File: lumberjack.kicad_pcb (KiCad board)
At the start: 2 copper layers, 284.7 x 94.2 mm, 164 parts, among them J1 USB, J2 AVR_ISP_6, J3 JST, J4 JST, SW1 RESET, SW2 BOOT, U1 ATMEGA328-PU, Y1 16MHz

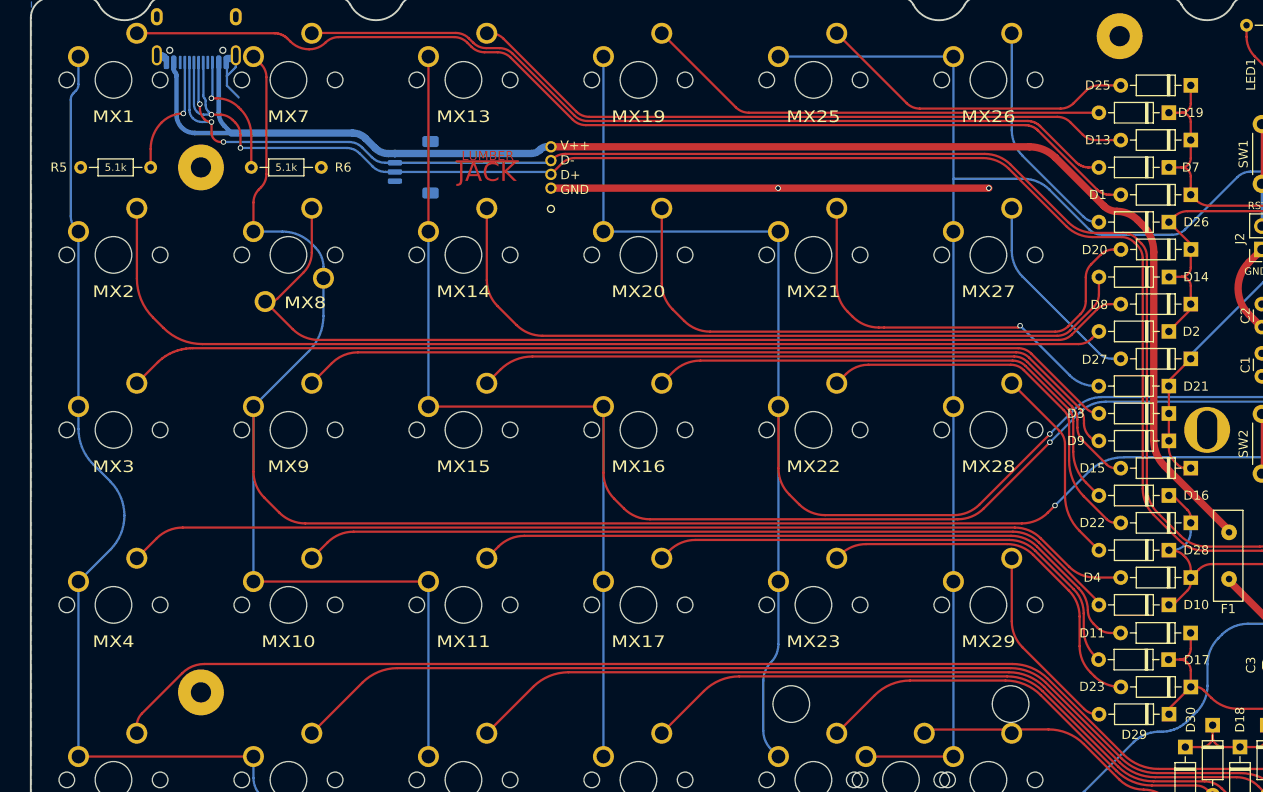
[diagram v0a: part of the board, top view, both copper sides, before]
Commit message: Add Molex connector footprint
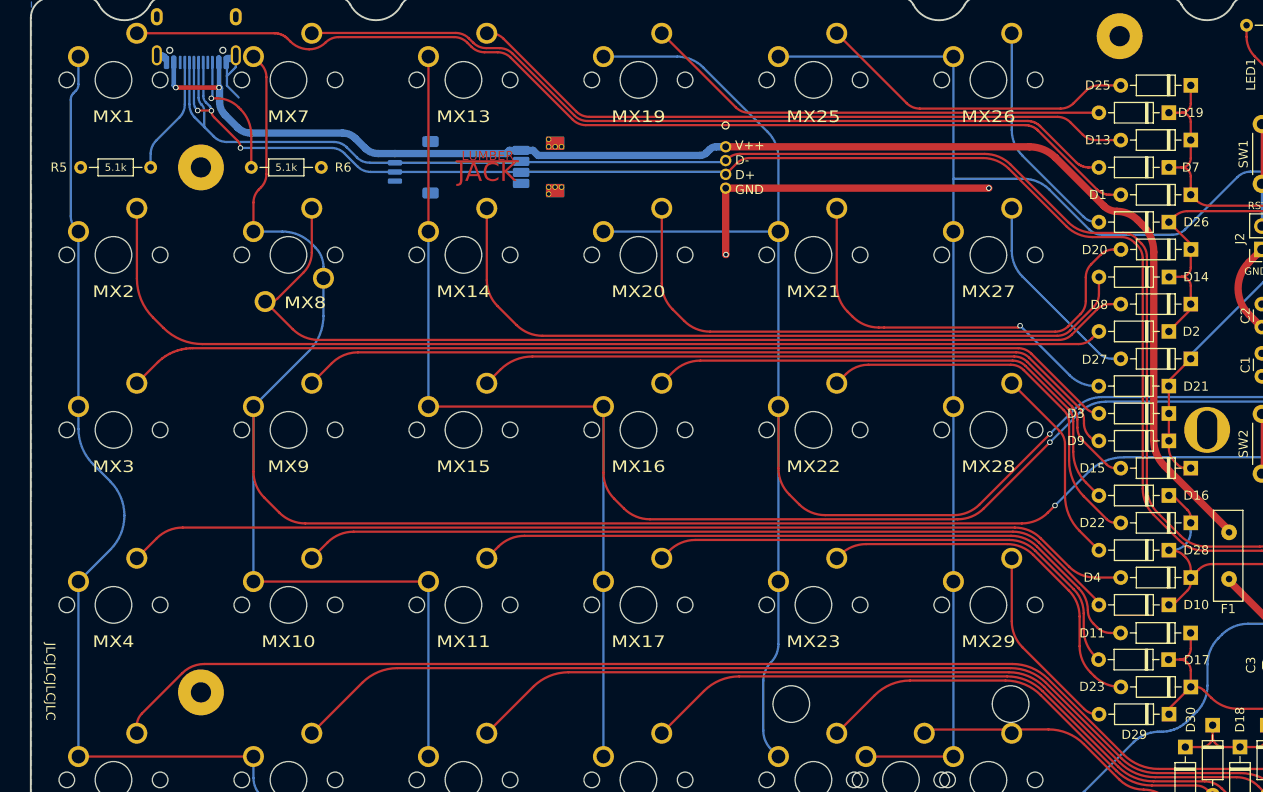
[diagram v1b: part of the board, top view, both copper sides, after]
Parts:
- added J5: Molex, lumberjack:PicoEZMate-Reinforced-Lite, B.Cu at (65.6, 73.8)
- moved J4 19.0 mm to (85.7, 76.1)
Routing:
- net /COL3: track 198.3 -> 211.5 mm
- net GND: track 94.6 -> 82.9 mm
- net Net-(J3-Pin_1): track 162.2 -> 156.6 mm, vias 0 -> 2
- net Net-(D61-K): track 187.2 -> 186.5 mm, vias 2 -> 3
- net Net-(J1-CC1): track 14.0 -> 13.3 mm, vias 1 -> 0
- net Net-(D62-K): track 189.2 -> 188.6 mm, vias 3 -> 0
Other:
- board text added: "MOLEX"

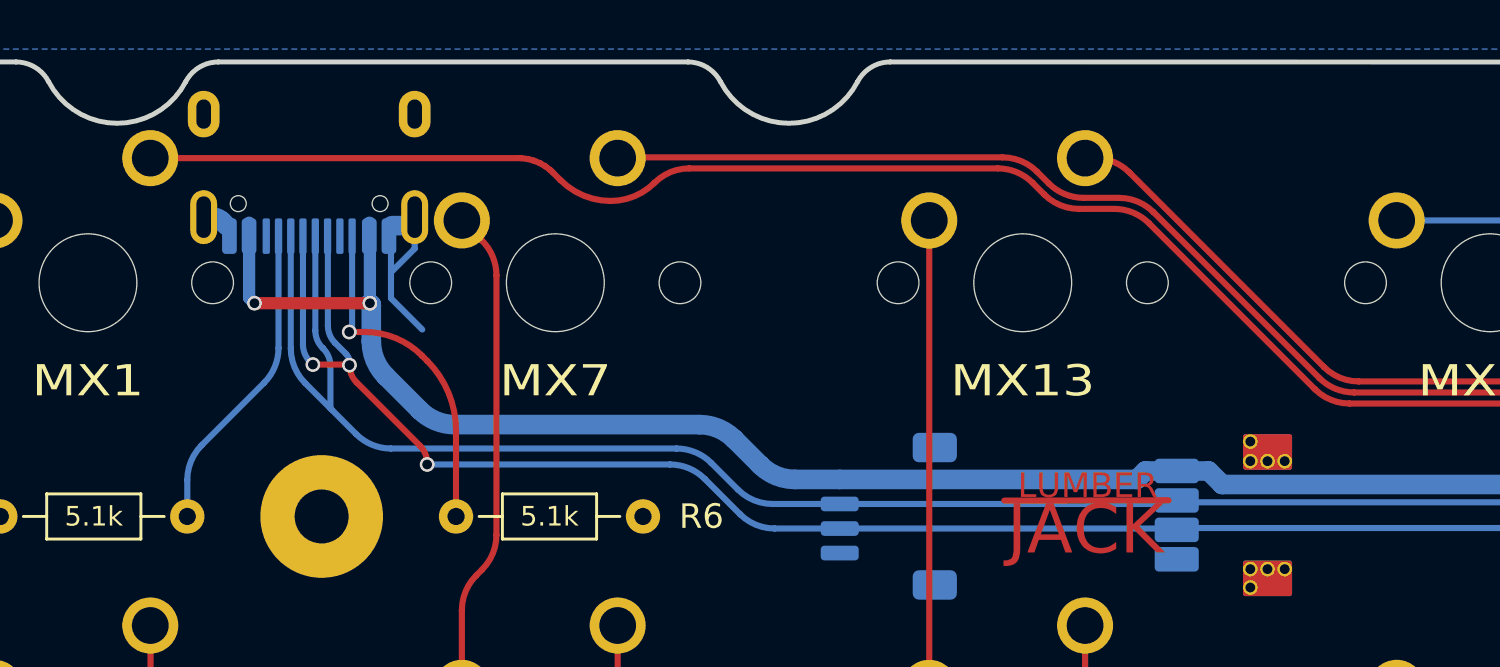
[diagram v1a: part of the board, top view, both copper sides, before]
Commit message: Move USB footprint closer to end of board
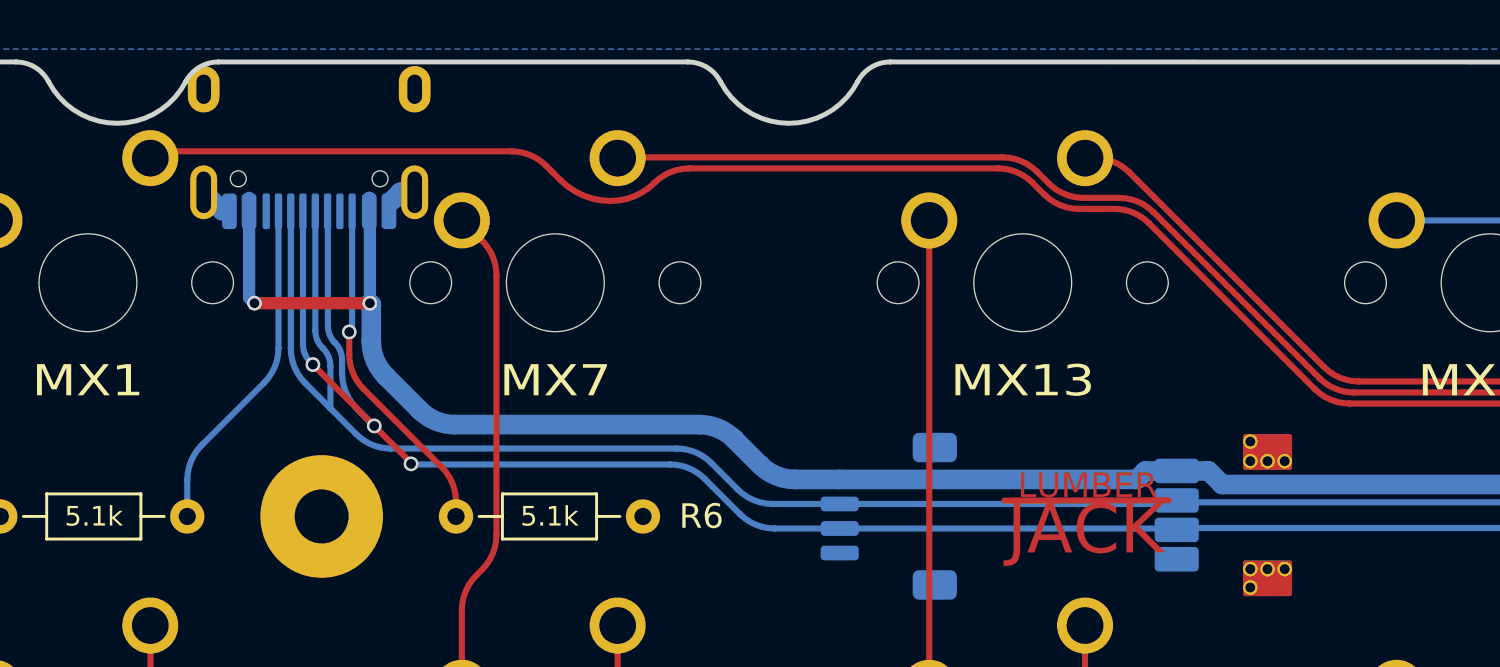
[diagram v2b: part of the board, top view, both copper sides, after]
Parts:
- moved J1 1.01 mm to (28.1, 62.1)
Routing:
- net GND: track 82.9 -> 75.3 mm
- net Net-(D61-K): track 186.5 -> 190.9 mm
- net Net-(J3-Pin_1): track 156.6 -> 159.6 mm
- net Net-(D62-K): track 188.6 -> 190.6 mm
- net Net-(J1-CC1): track 13.3 -> 14.3 mm
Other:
- board text added: "rev1.8 04/2024"
- board text removed: "rev1.8 03/2024"

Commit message: Add H60 compatible edge cutouts
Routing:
- net Net-(D7-A): track 90.3 -> 91.2 mm
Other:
- outline, holes or cut-outs redrawn
- board text added: "rev1.9 06/2024"
- board text removed: "rev1.8 04/2024"
